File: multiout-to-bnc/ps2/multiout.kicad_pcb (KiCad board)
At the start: 2 copper layers, 0 parts

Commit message: Add outline to edge cut layer
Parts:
- added AL: L, multiout:WIREPAD, B.Cu at (147.3, 101.6)
- added AR: R, multiout:WIREPAD, B.Cu at (148.8, 101.6)
- added B: B, multiout:WIREPAD, B.Cu at (141.4, 101.6)
- added C1: 0.1uF, Capacitor_SMD:C_0603_1608Metric, F.Cu at (147.3, 99.3)
- added C2: 0.1uF, Capacitor_SMD:C_0603_1608Metric, F.Cu at (136.8, 97.4)
- added CN1: AVCONNECTOR, multiout:AVCONNECTOR, F.Cu at (142.4, 94.3)
- added CS: CS, multiout:WIREPAD, B.Cu at (143.0, 101.6)
- added G: G, multiout:WIREPAD, B.Cu at (138.3, 101.6)
- added GND: GND, multiout:WIREPAD, F.Cu at (136.4, 101.6)
- added GND: GND, multiout:WIREPAD, F.Cu at (148.1, 101.6)
- added R: R, multiout:WIREPAD, B.Cu at (139.8, 101.6)
- added R1: 680k, Resistor_SMD:R_0603_1608Metric, F.Cu at (147.3, 97.5)
- added U1: LM1881, Package_SO:SOIC-8_3.9x4.9mm_P1.27mm, F.Cu at (141.7, 98.7)
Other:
- board outline added: 17.8 x 9.4 mm

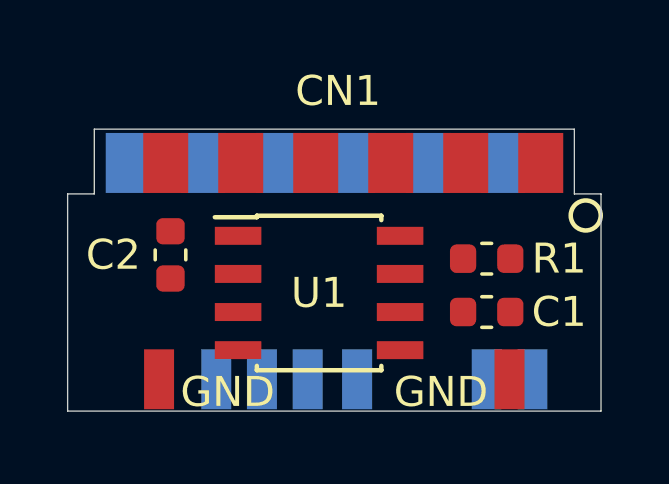
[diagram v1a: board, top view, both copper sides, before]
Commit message: Add routes to pcb
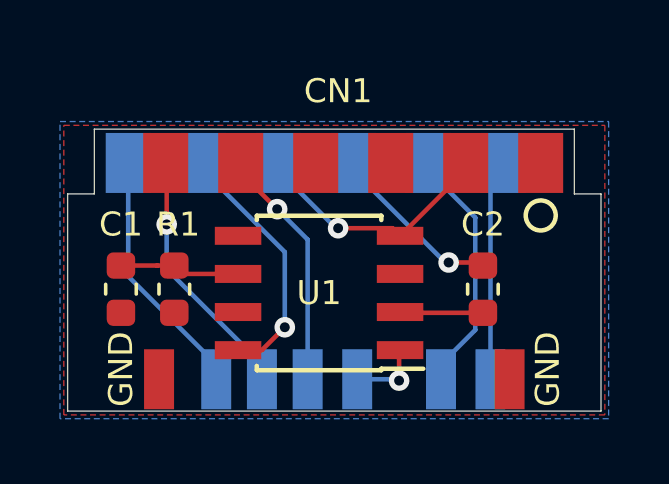
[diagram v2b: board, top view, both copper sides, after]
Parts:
- moved C1 12.2 mm to (135.1, 98.6), turned to 90 degrees
- moved C2 10.5 mm to (147.2, 98.6)
- moved R1 10.5 mm to (136.9, 98.6), turned to 90 degrees
- moved AR 3.05 mm to (145.8, 101.6)
- moved AL 0.13 mm to (147.4, 101.6)
- turned U1 to 180 degrees
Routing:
- net GND: track 0.00 -> 8.56 mm, vias 0 -> 1
- net Net-(CN1-Pad11): track 0.00 -> 8.54 mm, vias 0 -> 1
- net VCC: track 0.00 -> 8.48 mm, vias 0 -> 1
- net Net-(CN1-Pad12): track 0.00 -> 8.42 mm
- net Net-(CN1-Pad4): track 0.00 -> 8.33 mm
- net Net-(CN1-Pad9): track 0.00 -> 8.13 mm, vias 0 -> 1
- net Net-(CN1-Pad2): track 0.00 -> 7.39 mm
- net Net-(C2-Pad1): track 0.00 -> 5.89 mm, vias 0 -> 1
- net Net-(C1-Pad2): track 0.00 -> 4.02 mm
- net Net-(C2-Pad2): track 0.00 -> 2.77 mm
- net Net-(J3-Pad1): track 0.00 -> 2.45 mm, vias 0 -> 1
- added copper zone on B.Cu, net GND
- added copper zone on F.Cu, net GND

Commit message: Reroute after design changes to connector
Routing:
- net GND: track 8.56 -> 22.8 mm
- net Net-(CN1-Pad12): track 8.42 -> 9.10 mm

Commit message: Corrected placement of edge connector.
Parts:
- moved CN1 0.53 mm to (141.8, 94.3)
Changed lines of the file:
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@@
     (thickness 1.6)
     (drawings 8)
-    (tracks 68)
+    (tracks 70)
     (zones 0)
     (modules 13)
@@
   )
   (module multiout:AVCONNECTOR locked (layer F.Cu)
-    (at 142.37 94.345)
+    (at 141.836 94.345)
     (fp_text reference CN1 (at -0.003 -2.397) (layer F.SilkS)
       (effects (font (size 0.8 0.8) (thickness 0.15)))
@@
   (segment (start 148.082 96.6094) (end 148.082 100.4026) (width 0.1524) (layer F.Cu) (net 1))
   (segment (start 146.97 95.4974) (end 148.082 96.6094) (width 0.1524) (layer F.Cu) (net 1))
-  (segment (start 146.97 94.345) (end 146.97 95.4974) (width 0.1524) (layer F.Cu) (net 1))
   (segment (start 135.128 99.3395) (end 136.906 99.3395) (width 0.1524) (layer F.Cu) (net 1))
   (segment (start 136.398 99.8475) (end 136.906 99.3395) (width 0.1524) (layer F.Cu) (net 1))
   (segment (start 136.398 101.555) (end 136.398 99.8475) (width 0.1524) (layer F.Cu) (net 1))
-  (segment (start 146.97 94.345) (end 149.37 94.345) (width 0.1524) (layer F.Cu) (net 1))
-  (segment (start 141.7224 94.345) (end 140.97 94.345) (width 0.1524) (layer B.Cu) (net 1))
-  (segment (start 142.367 94.9896) (end 141.7224 94.345) (width 0.1524) (layer B.Cu) (net 1))
-  (segment (start 142.367 96.52) (end 142.367 94.9896) (width 0.1524) (layer B.Cu) (net 1))
+  (segment (start 140.436 94.589) (end 140.436 94.345) (width 0.1524) (layer B.Cu) (net 1))
+  (segment (start 142.367 96.52) (end 140.436 94.589) (width 0.1524) (layer B.Cu) (net 1))
+  (segment (start 148.0836 94.345) (end 148.836 94.345) (width 0.1524) (layer F.Cu) (net 1))
+  (segment (start 146.97 95.4586) (end 148.0836 94.345) (width 0.1524) (layer F.Cu) (net 1))
+  (segment (start 146.97 95.4974) (end 146.97 95.4586) (width 0.1524) (layer F.Cu) (net 1))
+  (segment (start 146.97 94.879) (end 146.436 94.345) (width 0.1524) (layer F.Cu) (net 1))
+  (segment (start 146.97 95.4974) (end 146.97 94.879) (width 0.1524) (layer F.Cu) (net 1))
   (segment (start 137.1855 98.044) (end 136.906 97.7645) (width 0.1524) (layer F.Cu) (net 2))
   (segment (start 139.032 98.044) (end 137.1855 98.044) (width 0.1524) (layer F.Cu) (net 2))
@@
   (segment (start 146.05 97.663) (end 147.0915 97.663) (width 0.1524) (layer F.Cu) (net 4))
   (segment (start 146.05 97.663) (end 145.415 97.663) (width 0.1524) (layer B.Cu) (net 4))
-  (segment (start 143.37 95.618) (end 143.37 94.345) (width 0.1524) (layer B.Cu) (net 4))
-  (segment (start 145.415 97.663) (end 143.37 95.618) (width 0.1524) (layer B.Cu) (net 4))
+  (segment (start 142.836 94.745) (end 142.836 94.345) (width 0.1524) (layer B.Cu) (net 4))
+  (segment (start 145.415 97.324) (end 142.836 94.745) (width 0.1524) (layer B.Cu) (net 4))
+  (segment (start 145.415 97.663) (end 145.415 97.324) (width 0.1524) (layer B.Cu) (net 4))
   (via (at 140.335 95.885) (size 0.6858) (drill 0.3302) (layers F.Cu B.Cu) (net 5))
   (segment (start 141.351 101.555) (end 141.351 96.901) (width 0.1524) (layer B.Cu) (net 5))
   (segment (start 141.351 96.901) (end 140.335 95.885) (width 0.1524) (layer B.Cu) (net 5))
-  (segment (start 139.77 94.835067) (end 139.77 94.345) (width 0.1524) (layer F.Cu) (net 5))
-  (segment (start 140.335 95.400067) (end 139.77 94.835067) (width 0.1524) (layer F.Cu) (net 5))
-  (segment (start 140.335 95.885) (end 140.335 95.400067) (width 0.1524) (layer F.Cu) (net 5))
+  (segment (start 140.335 95.844) (end 140.335 95.885) (width 0.1524) (layer F.Cu) (net 5))
+  (segment (start 139.236 94.745) (end 140.335 95.844) (width 0.1524) (layer F.Cu) (net 5))
+  (segment (start 139.236 94.345) (end 139.236 94.745) (width 0.1524) (layer F.Cu) (net 5))
   (via (at 136.652 96.393) (size 0.6858) (drill 0.3302) (layers F.Cu B.Cu) (net 6))
   (segment (start 136.652 97.88) (end 136.652 96.393) (width 0.1524) (layer B.Cu) (net 6))
   (segment (start 139.827 101.555) (end 139.827 101.055) (width 0.1524) (layer B.Cu) (net 6))
   (segment (start 139.827 101.055) (end 136.652 97.88) (width 0.1524) (layer B.Cu) (net 6))
-  (segment (start 137.37 95.675) (end 137.37 94.345) (width 0.1524) (layer F.Cu) (net 6))
-  (segment (start 136.652 96.393) (end 137.37 95.675) (width 0.1524) (layer F.Cu) (net 6))
-  (segment (start 136.17 94.745) (end 136.17 94.345) (width 0.1524) (layer B.Cu) (net 7))
-  (segment (start 135.4176 95.4974) (end 136.17 94.745) (width 0.1524) (layer B.Cu) (net 7))
-  (segment (start 135.4176 99.322) (end 135.4176 95.4974) (width 0.1524) (layer B.Cu) (net 7))
+  (segment (start 136.836 96.209) (end 136.652 96.393) (width 0.1524) (layer F.Cu) (net 6))
+  (segment (start 136.836 94.345) (end 136.836 96.209) (width 0.1524) (layer F.Cu) (net 6))
+  (segment (start 135.4176 94.5634) (end 135.636 94.345) (width 0.1524) (layer B.Cu) (net 7))
+  (segment (start 135.4176 99.322) (end 135.4176 94.5634) (width 0.1524) (layer B.Cu) (net 7))
+  (segment (start 138.303 101.555) (end 137.6506 101.555) (width 0.1524) (layer B.Cu) (net 7))
   (segment (start 137.6506 101.555) (end 135.4176 99.322) (width 0.1524) (layer B.Cu) (net 7))
-  (segment (start 138.303 101.555) (end 137.6506 101.555) (width 0.1524) (layer B.Cu) (net 7))
   (segment (start 145.37 94.595) (end 145.37 94.345) (width 0.1524) (layer B.Cu) (net 8))
-  (segment (start 145.77 95.4974) (end 145.77 94.345) (width 0.1524) (layer B.Cu) (net 8))
-  (segment (start 146.621501 96.348901) (end 145.77 95.4974) (width 0.1524) (layer B.Cu) (net 8))
-  (segment (start 146.621501 99.577099) (end 146.621501 96.348901) (width 0.1524) (layer B.Cu) (net 8))
+  (segment (start 145.236 94.745) (end 145.236 94.345) (width 0.1524) (layer B.Cu) (net 8))
+  (segment (start 146.621501 96.130501) (end 145.236 94.745) (width 0.1524) (layer B.Cu) (net 8))
+  (segment (start 146.621501 99.577099) (end 146.621501 96.130501) (width 0.1524) (layer B.Cu) (net 8))
   (segment (start 145.796 100.4026) (end 146.621501 99.577099) (width 0.1524) (layer B.Cu) (net 8))
   (segment (start 145.796 101.555) (end 145.796 100.4026) (width 0.1524) (layer B.Cu) (net 8))
@@
   (segment (start 139.827 100.584) (end 139.032 100.584) (width 0.1524) (layer F.Cu) (net 9))
   (segment (start 140.589 99.822) (end 139.827 100.584) (width 0.1524) (layer F.Cu) (net 9))
-  (segment (start 138.57 97.803) (end 140.589 99.822) (width 0.1524) (layer B.Cu) (net 9))
-  (segment (start 138.57 94.345) (end 138.57 97.803) (width 0.1524) (layer B.Cu) (net 9))
-  (segment (start 147.447 95.068) (end 148.17 94.345) (width 0.1524) (layer B.Cu) (net 10))
-  (segment (start 147.447 101.555) (end 147.447 95.068) (width 0.1524) (layer B.Cu) (net 10))
+  (segment (start 138.036 97.269) (end 138.036 94.345) (width 0.1524) (layer B.Cu) (net 9))
+  (segment (start 140.589 99.822) (end 138.036 97.269) (width 0.1524) (layer B.Cu) (net 9))
+  (segment (start 147.447 94.534) (end 147.636 94.345) (width 0.1524) (layer B.Cu) (net 10))
+  (segment (start 147.447 101.555) (end 147.447 94.534) (width 0.1524) (layer B.Cu) (net 10))
   (via (at 144.399 101.6) (size 0.6858) (drill 0.3302) (layers F.Cu B.Cu) (net 11))
   (segment (start 143.002 101.555) (end 144.354 101.555) (width 0.1524) (layer B.Cu) (net 11))
